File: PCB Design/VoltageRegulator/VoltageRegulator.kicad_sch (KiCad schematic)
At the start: 6 parts, among them J1 Screw_Terminal_01x08, U1 LM7815_TO220, U2 LM7806_TO220

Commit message: Schematic Rev C
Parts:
- added C2: 0.1uF, Capacitor_THT:CP_Radial_Tantal_D4.5mm_P2.50mm, symbol Device:C_Polarized_Small_US
- added C5: 56 uF, Capacitor_THT:CP_Radial_Tantal_D4.5mm_P2.50mm, symbol Device:C_Polarized_Small_US
- added C6: 1uF, Capacitor_THT:CP_Radial_Tantal_D4.5mm_P2.50mm, symbol Device:C_Polarized_Small_US
- added C7, C8: 6.6 uF, Capacitor_THT:CP_Radial_Tantal_D4.5mm_P2.50mm, symbol Device:C_Polarized_Small_US
- added J2: Conn_Coaxial, symbol Connector:Conn_Coaxial
- added J3: Screw_Terminal_01x01, symbol Connector:Screw_Terminal_01x01
- added L1: 4.7 uH, symbol Device:L
- added L2, L3: 2.2 uH, symbol Device:L
- added PS1: PQQ6W-Q24-D15-S, CONV_PQQ6W-Q24-D15-S, symbol PQQ6W-Q24-D15-S:PQQ6W-Q24-D15-S
- added R1: R_US, symbol Device:R_US
- added RV1: R_Potentiometer_US, symbol Device:R_Potentiometer_US
- added U4: OP27GPZ, N_8_ADI, symbol OP27GPZ:OP27GPZ
- renumbered C2 to C3, C3 to C4
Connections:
- net +15VDC: now also C2.1
- net +28V: now also C5.1, L1.1
- net GND: now also C2.2, C5.2, C6.2, C7.2, C8.1, PS1.1 (GND), PS1.7 (0V)
- new net: J3.1 (Pin_1), RV1.2, U4.6 (OUT)
- new net: R1.1, RV1.1, U4.2 (-IN)
- new net: J2.2 (Ext), U4.3 (+IN)
- new net: L3.1, PS1.8 (-VOUT)
- new net: C6.1, L1.2, PS1.2 (VIN)
- new net: L2.1, PS1.6 (+VOUT)
- new net: J2.1 (In), R1.2
- new net +15VLP: C7.1, L2.2, U4.7 (V+)
- new net -15VLP: C8.2, L3.2, U4.4 (V-)
- no-connect marks 0 -> 5
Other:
- note added: "28VDC to 15VDC to 6VDC Converter and Inverting Op-Amp"
- note added: "6/26/2023"
- note added: "C"
- note removed: "28VDC to 15VDC to 6VDC Converter"
- note removed: "6/16/2023"
- note removed: "B"
- moved on the sheet: C1, C3, C4, J1, U1, U2

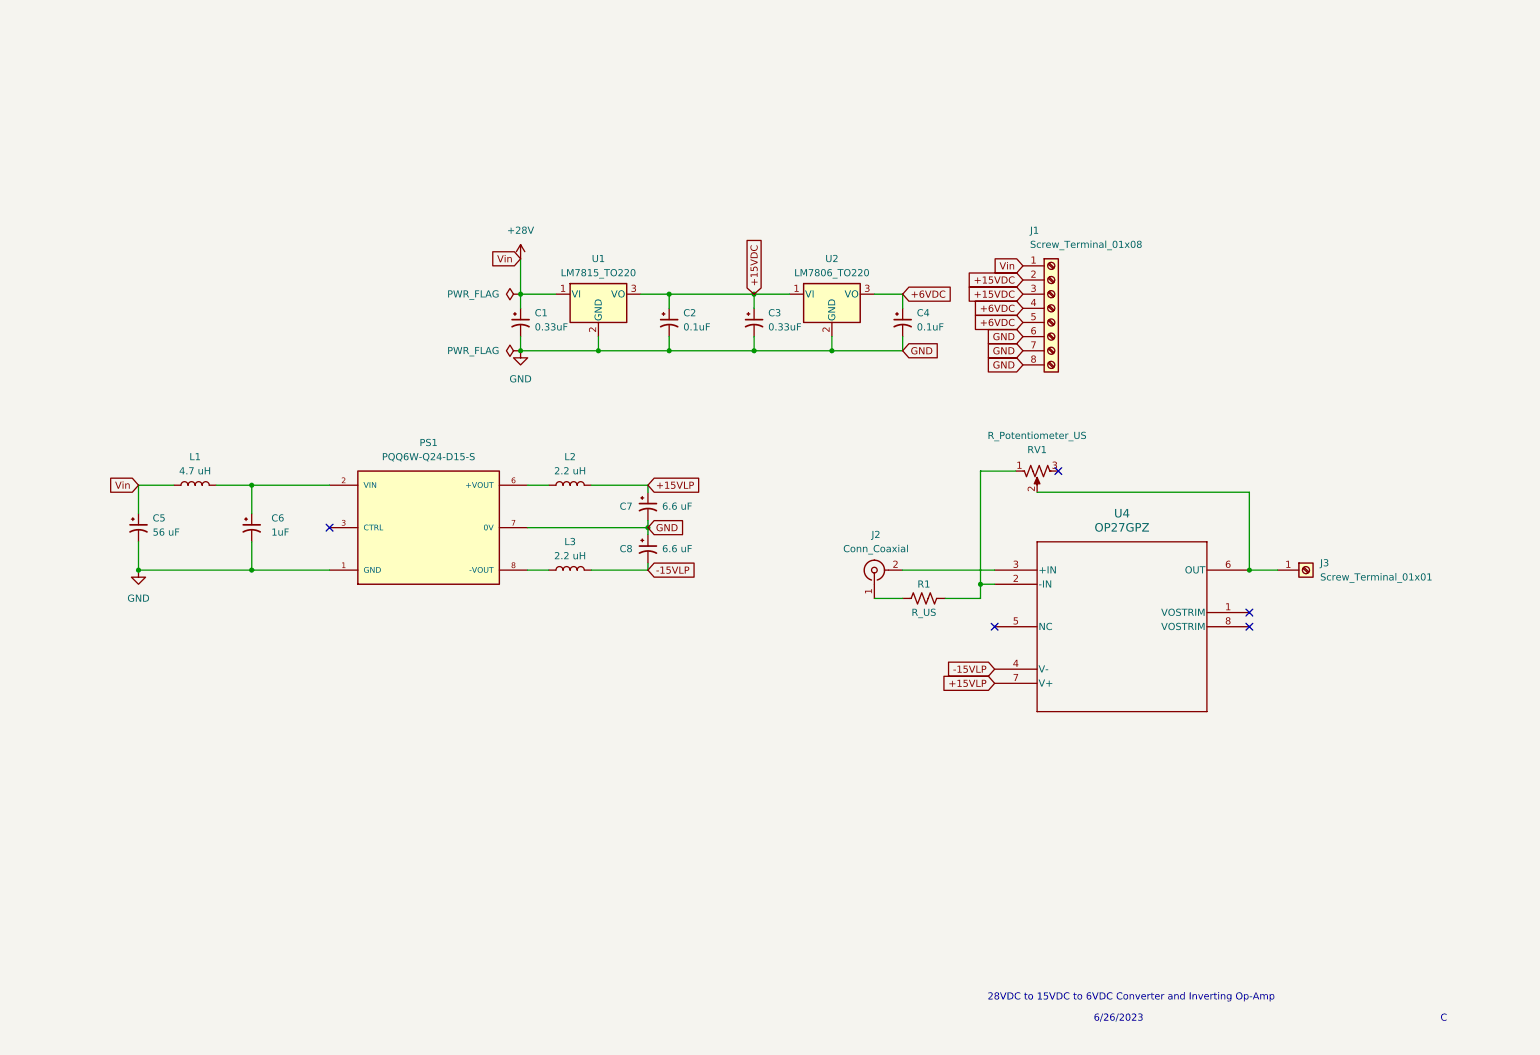
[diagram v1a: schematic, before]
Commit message: Schematic Revision C - AD8317
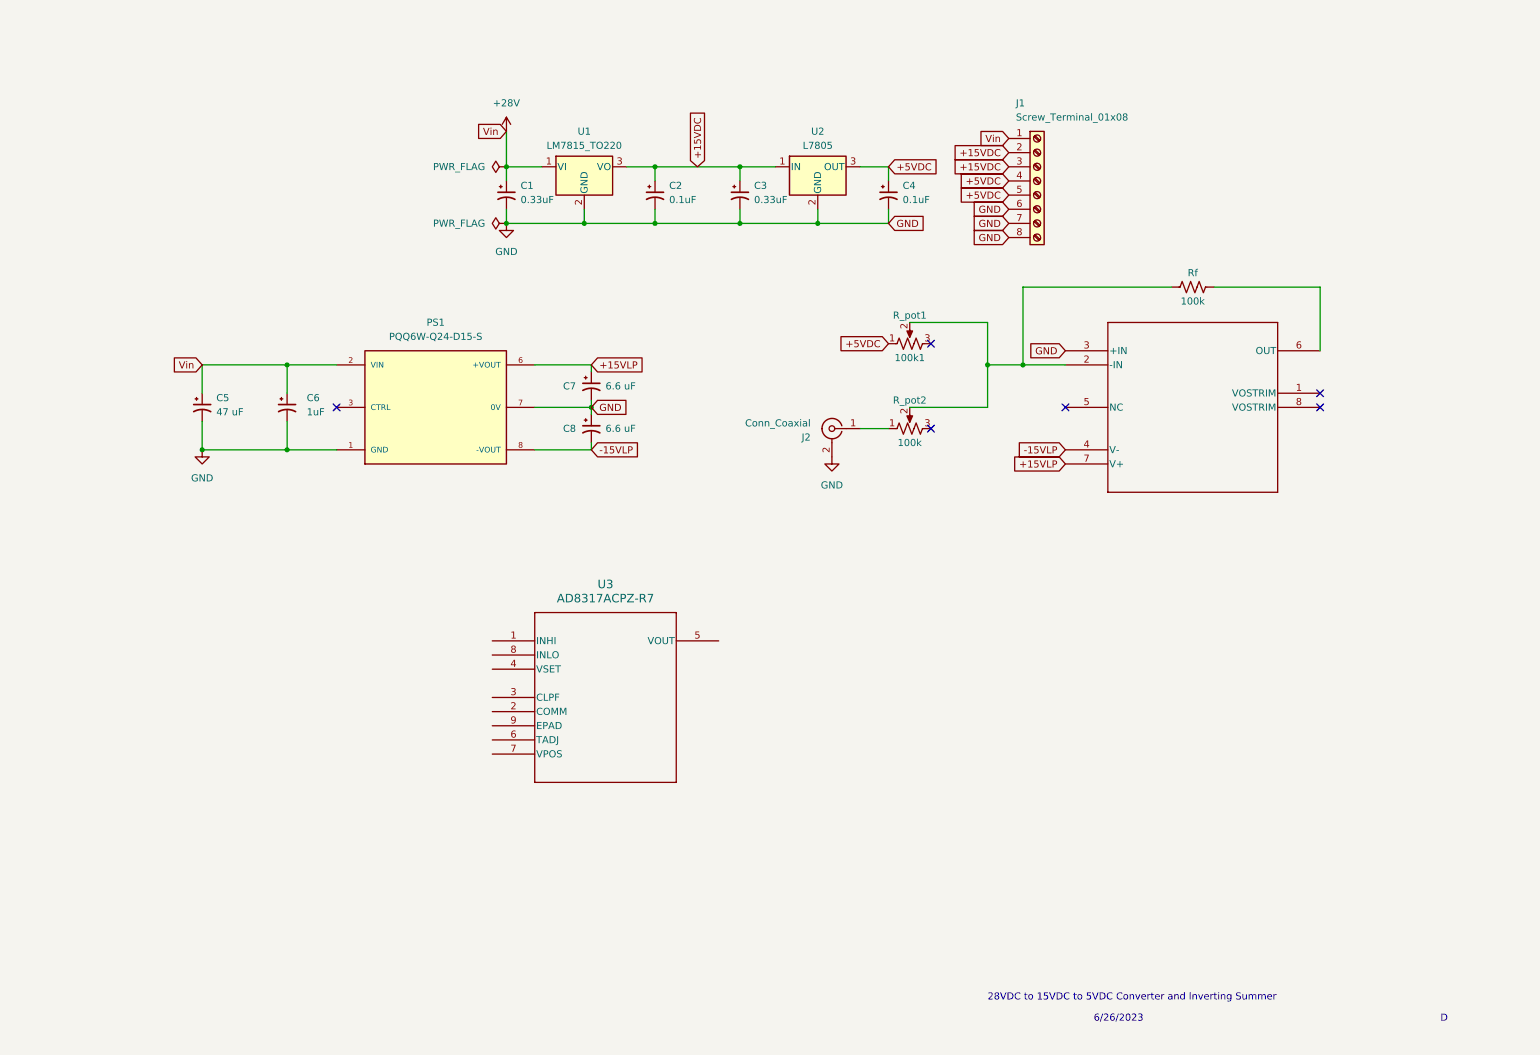
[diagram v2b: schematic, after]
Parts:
- removed J3: Screw_Terminal_01x01, symbol Connector:Screw_Terminal_01x01
- removed L1: 4.7 uH, symbol Device:L
- removed L2, L3: 2.2 uH, symbol Device:L
- removed R1: R_US, symbol Device:R_US
- removed RV1: R_Potentiometer_US, symbol Device:R_Potentiometer_US
- removed U2: LM7806_TO220, Package_TO_SOT_THT:TO-220-3_Horizontal_TabDown, symbol Regulator_Linear:LM7806_TO220
- added 100k: R_pot2, symbol Device:R_Potentiometer_US
- added 100k1: R_pot1, symbol Device:R_Potentiometer_US
- added Rf: 100k, symbol Device:R_US
- added U2: L7805, symbol Regulator_Linear:L7805
- added U3: AD8317ACPZ-R7, CP_8_1_ADI, symbol AD8317ACPZ-R7:AD8317ACPZ-R7
- C5: value 56 uF -> 47 uF
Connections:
- net +15VDC: now also U2.1 (IN)
- net +15VLP: now also PS1.6 (+VOUT)
- net +28V: now also C6.1, PS1.2 (VIN)
- net -15VLP: now also PS1.8 (-VOUT)
- net GND: now also J2.2 (Ext), U4.3 (+IN), U2.2 (GND)
- net at U4.6 (OUT): now also Rf.2
- net at U4.2 (-IN): now also 100k.2, 100k1.2, Rf.1
- net at J2.1 (In): now also 100k.1
- net +6VDC renamed +5VDC
- net +5VDC: now also 100k1.1, U2.3 (OUT)
- no-connect marks 5 -> 6
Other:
- note added: "28VDC to 15VDC to 5VDC Converter and Inverting Summer"
- note added: "D"
- note removed: "28VDC to 15VDC to 6VDC Converter and Inverting Op-Amp"
- note removed: "C"
- moved on the sheet: C1, C2, C3, C4, C5, C6, C7, C8, J1, PS1, U1

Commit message: Schematic Revision D Draft, Datasheets added
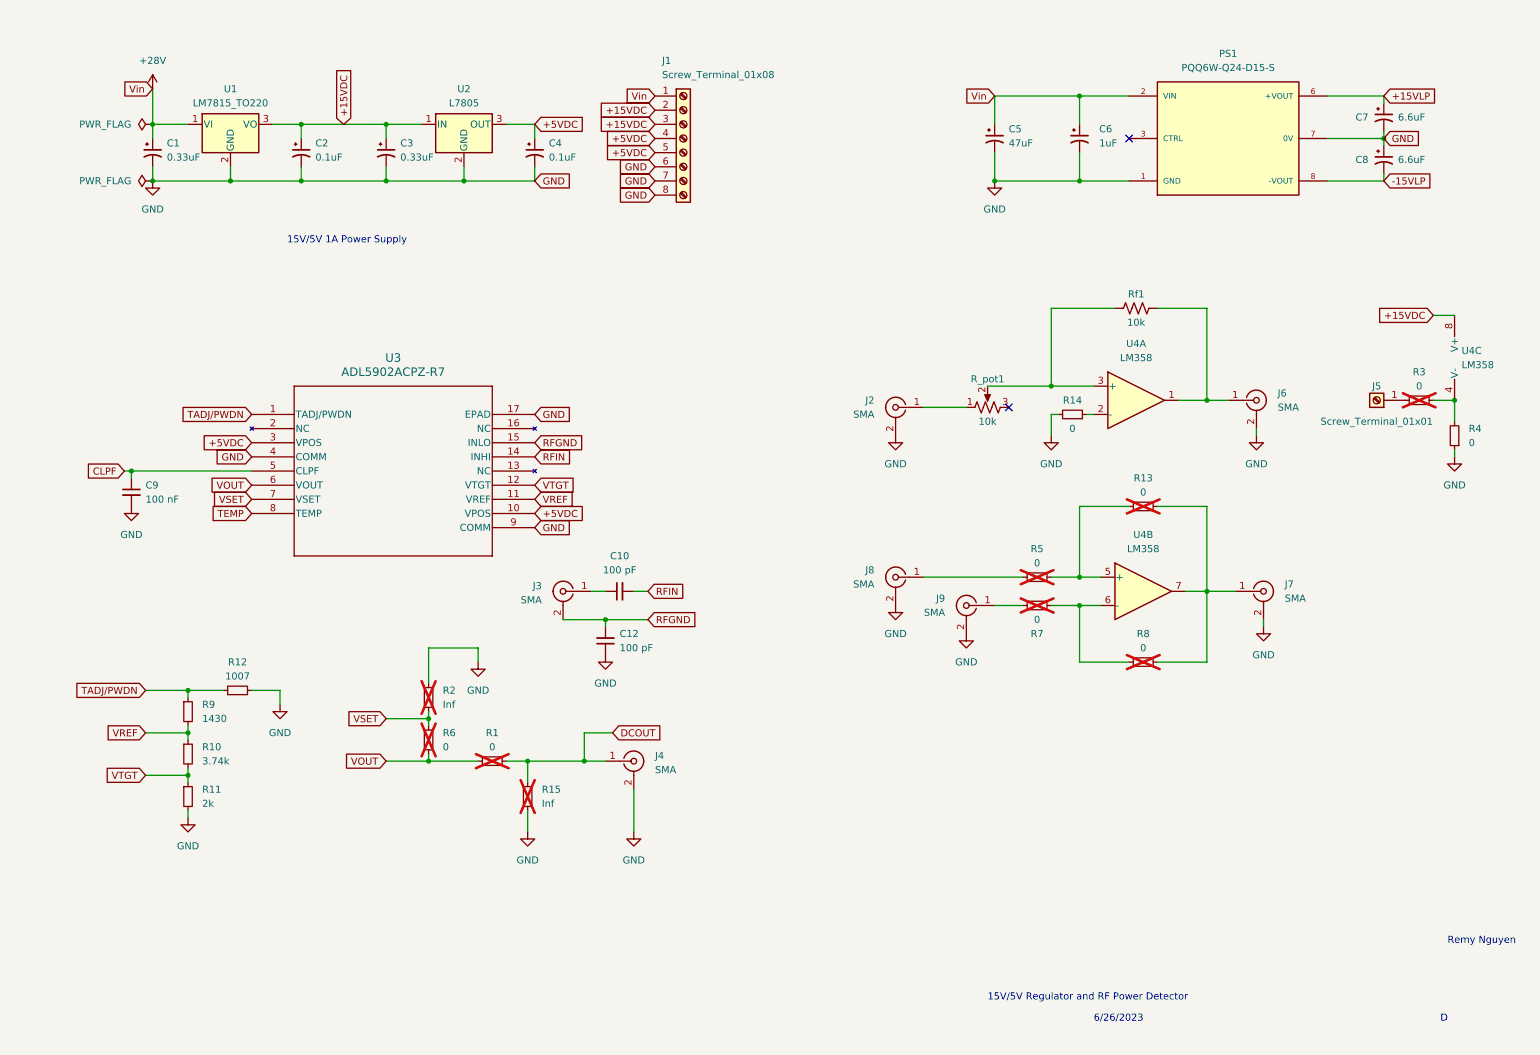
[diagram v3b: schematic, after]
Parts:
- removed 100k1: R_pot1, symbol Device:R_Potentiometer_US
- removed U3: AD8317ACPZ-R7, CP_8_1_ADI, symbol AD8317ACPZ-R7:AD8317ACPZ-R7
- removed U4: OP27GPZ, N_8_ADI, symbol OP27GPZ:OP27GPZ
- added C10, C12: 100 pF, symbol Device:C_Small
- added C9: 100 nF, symbol Device:C_Small
- added J3, J4, J6, J7, J8, J9: SMA, symbol Connector:Conn_Coaxial
- added J5: Screw_Terminal_01x01, Connector_Phoenix_SPT:PhoenixContact_SPT_5_1-V-7.5_1x01_P7.5mm_Vertical, symbol Connector:Screw_Terminal_01x01
- added R1, R13, R14, R3, R4, R5, R6, R7, R8: 0, symbol Device:R_Small
- added R10: 3.74k, symbol Device:R_Small
- added R11: 2k, symbol Device:R_Small
- added R12: 1007, symbol Device:R_Small
- added R15, R2: Inf, symbol Device:R_Small
- added R9: 1430, symbol Device:R_Small
- added U3: ADL5902ACPZ-R7, CP_16_20_ADI, symbol AD5902ACPZ-R7:ADL5902ACPZ-R7
- added U4: LM358, symbol Amplifier_Operational:LM358
- C5: value 47 uF -> 47uF
- C7, C8: value 6.6 uF -> 6.6uF
- J2: value Conn_Coaxial -> SMA
- R_pot1: renamed from 100k; value R_pot2 -> 10k
- Rf1: renamed from Rf; value 100k -> 10k
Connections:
- net +15VDC: now also U4.8 (V+)
- net +5VDC: now also U3.10 (VPOS), U3.3 (VPOS)
- net GND: now also C12.1, C9.2, J4.2 (Ext), J6.2 (Ext), J7.2 (Ext), J8.2 (Ext), J9.2 (Ext), R11.2, R12.2, R14.2, R15.2, R2.1, R4.1, U3.17 (EPAD), U3.4 (COMM), U3.9 (COMM)
- net at R_pot1.2, Rf1.1: now also U4.3 (+)
- net at Rf1.2: now also J6.1 (In), U4.1
- new net: R14.1, U4.2 (-)
- new net: J7.1 (In), R13.1, R8.1, U4.7
- new net: R13.2, R5.2, U4.5 (+)
- new net: R3.2, R4.2, U4.4 (V-)
- new net: J9.1 (In), R7.1
- new net: J5.1 (Pin_1), R3.1
- new net: R7.2, R8.2, U4.6 (-)
- new net: J8.1 (In), R5.1
- new net: C10.1, J3.1 (In)
- new net CLPF: C9.1, U3.5 (CLPF)
- new net DCOUT: J4.1 (In), R1.2, R15.1
- new net RFGND: C12.2, J3.2 (Ext), U3.15 (INLO)
- new net RFIN: C10.2, U3.14 (INHI)
- new net TADJ/PWDN: R12.1, R9.1, U3.1 (TADJ/PWDN)
- new net TEMP: U3.8 (TEMP)
- new net VOUT: R1.1, R6.2, U3.6 (VOUT)
- new net VREF: R10.1, R9.2, U3.11 (VREF)
- new net VSET: R2.2, R6.1, U3.7 (VSET)
- new net VTGT: R10.2, R11.1, U3.12 (VTGT)
- no-connect marks 6 -> 2
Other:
- note added: "15V/5V 1A Power Supply"
- note added: "15V/5V Regulator and RF Power Detector"
- note added: "Remy Nguyen"
- note removed: "28VDC to 15VDC to 5VDC Converter and Inverting Summer"
- moved on the sheet: C1, C2, C3, C4, C5, C6, C7, C8, J1, J2, PS1, R_pot1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

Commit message: Schematic Rev C complete, ADL5902 pins reassigned; ERC pass
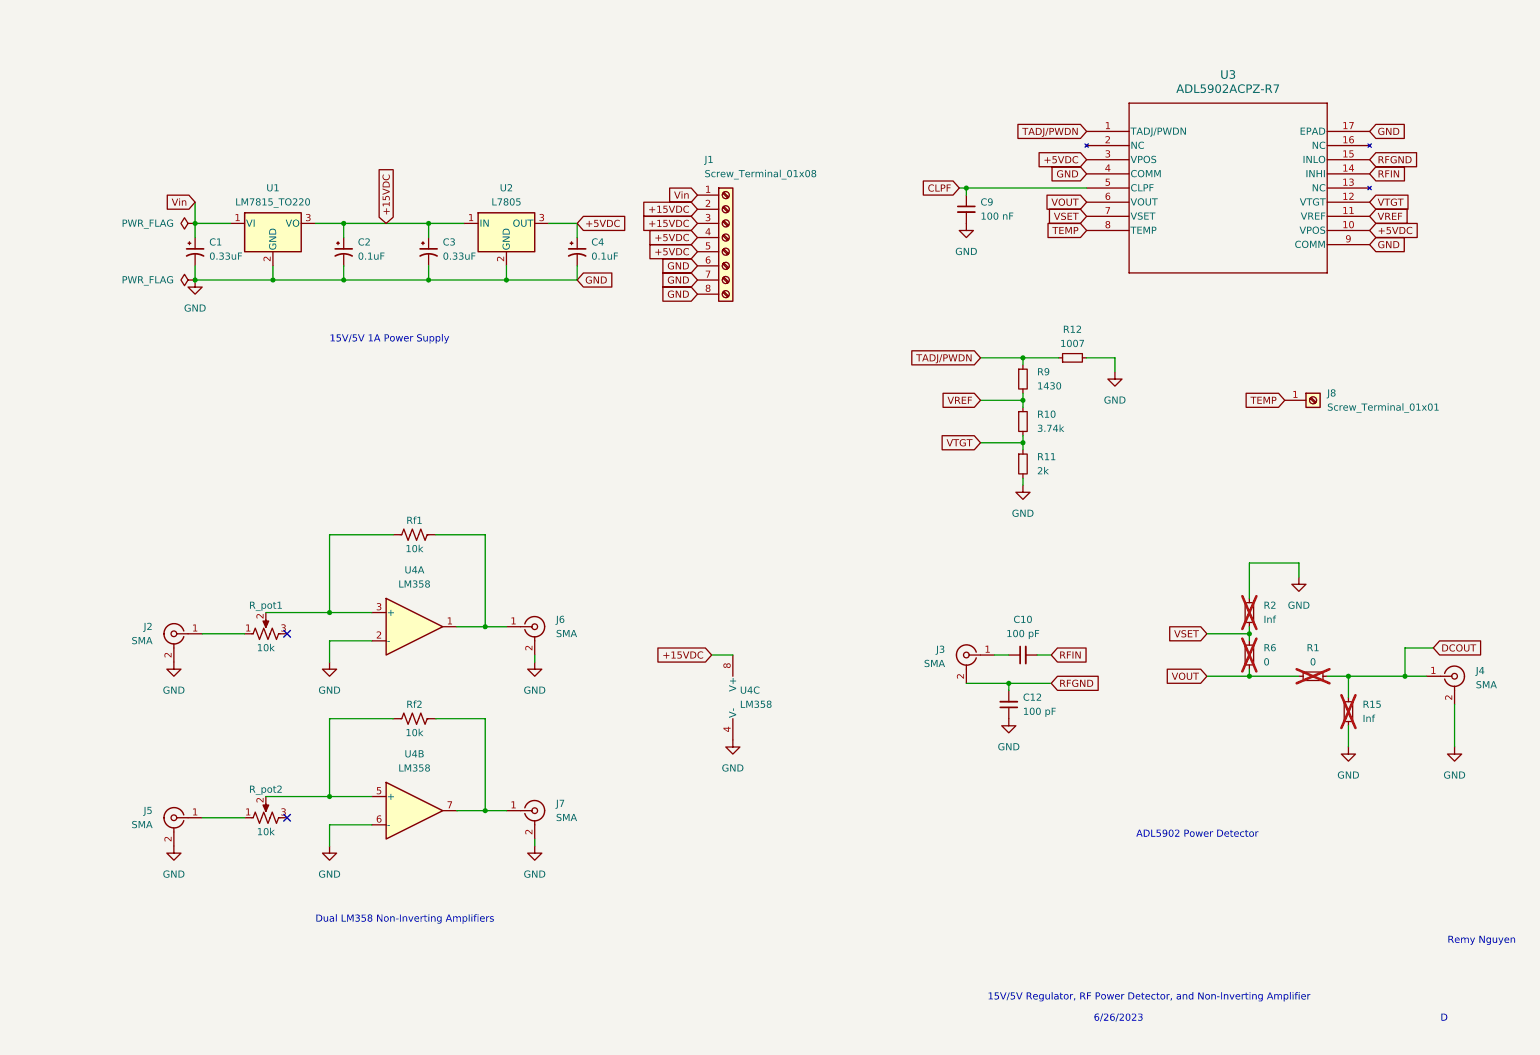
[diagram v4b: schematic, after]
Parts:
- removed C5: 47uF, Capacitor_THT:CP_Radial_Tantal_D4.5mm_P2.50mm, symbol Device:C_Polarized_Small_US
- removed C6: 1uF, Capacitor_THT:CP_Radial_Tantal_D4.5mm_P2.50mm, symbol Device:C_Polarized_Small_US
- removed C7, C8: 6.6uF, Capacitor_THT:CP_Radial_Tantal_D4.5mm_P2.50mm, symbol Device:C_Polarized_Small_US
- removed J5: Screw_Terminal_01x01, Connector_Phoenix_SPT:PhoenixContact_SPT_5_1-V-7.5_1x01_P7.5mm_Vertical, symbol Connector:Screw_Terminal_01x01
- removed J8, J9: SMA, symbol Connector:Conn_Coaxial
- removed PS1: PQQ6W-Q24-D15-S, CONV_PQQ6W-Q24-D15-S, symbol PQQ6W-Q24-D15-S:PQQ6W-Q24-D15-S
- removed R13, R14, R3, R4, R5, R7, R8: 0, symbol Device:R_Small
- added J5: SMA, symbol Connector:Conn_Coaxial
- added J8: Screw_Terminal_01x01, symbol Connector:Screw_Terminal_01x01
- added R_pot2: 10k, symbol Device:R_Potentiometer_US
- added Rf2: 10k, symbol Device:R_US
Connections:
- net GND: now also U4.2 (-), U4.4 (V-), U4.6 (-), J5.2 (Ext)
- net TEMP: now also J8.1 (Pin_1)
- net at J7.1 (In), U4.7: now also Rf2.2
- net at U4.5 (+): now also R_pot2.2, Rf2.1
- net +28V renamed Vin
- new net: J5.1 (In), R_pot2.1
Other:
- note added: "15V/5V Regulator, RF Power Detector, and Non-Inverting Amplifier"
- note added: "ADL5902 Power Detector"
- note added: "Dual LM358 Non-Inverting Amplifiers"
- note removed: "15V/5V Regulator and RF Power Detector"
- moved on the sheet: C1, C10, C12, C2, C3, C4, C9, J1, J2, J3, J4, J6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
